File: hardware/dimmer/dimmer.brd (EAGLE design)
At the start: 112.1 x 40.6 mm, 34 parts, among them IC1 MEGA48/88/168-PU, IC2 RFM12, IC3 7812L, IC4 LP2950Z, K1 G5LE, T1 BC547, T2 BC547, X1 AC In, X2 DIM Out, X3 AC Out

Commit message: update labels
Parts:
- D1, D2, D3, D4, D5, D6: value 1N4148DO35-7 -> 1N4148
- JP3: value TX -> PD1/TX
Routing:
- net N$19: track 47.0 -> 48.3 mm
- added copper zone on layer 1, net GND
- added copper zone on layer 16, net GND
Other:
- board text added: "+"
- board text added: "Dimmer 1"
- board text removed: "Dimmer"

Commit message: Use 1k3 instead of 1k2 resistor (0,1%), which is more common. Adopt lookup table accordingly. Change power off timeout to 3s.
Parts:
- C3: value 220n -> 100µ; device rcl:C025-030X050 -> rcl:E1,8-4
- F1: value F50mA -> T50mA; device fuse:GSH15 -> fuse:SH22,5
- IC1: value MEGA48/88/168-PU -> MEGA328PU
- R3: value 1k2 -> 1k3
- moved F1 5.09 mm to (8.57, 15.2)
- moved X3 2.54 mm to (0.00, 25.4)
- moved X1 2.54 mm to (0.00, 15.2)
- moved C2 1.27 mm to (62.2, 12.7), turned to 180 degrees
- turned C3 to 180 degrees
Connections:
- net GND: now also C3.-; no longer C3.2
- net N$9: now also C3.+; no longer C3.1
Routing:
- net N$19: track 48.3 -> 31.4 mm
- net N$22: track 54.6 -> 62.2 mm
- net GND: track 271.6 -> 277.2 mm
- net N$17: track 96.2 -> 91.9 mm
- net N$23: track 18.0 -> 13.9 mm
- net N$9: track 56.8 -> 55.4 mm
- net N$21: track 26.1 -> 25.0 mm
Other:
- board text added: "-"
- board text added: "1"
- board text added: "L"
- board text added: "N"

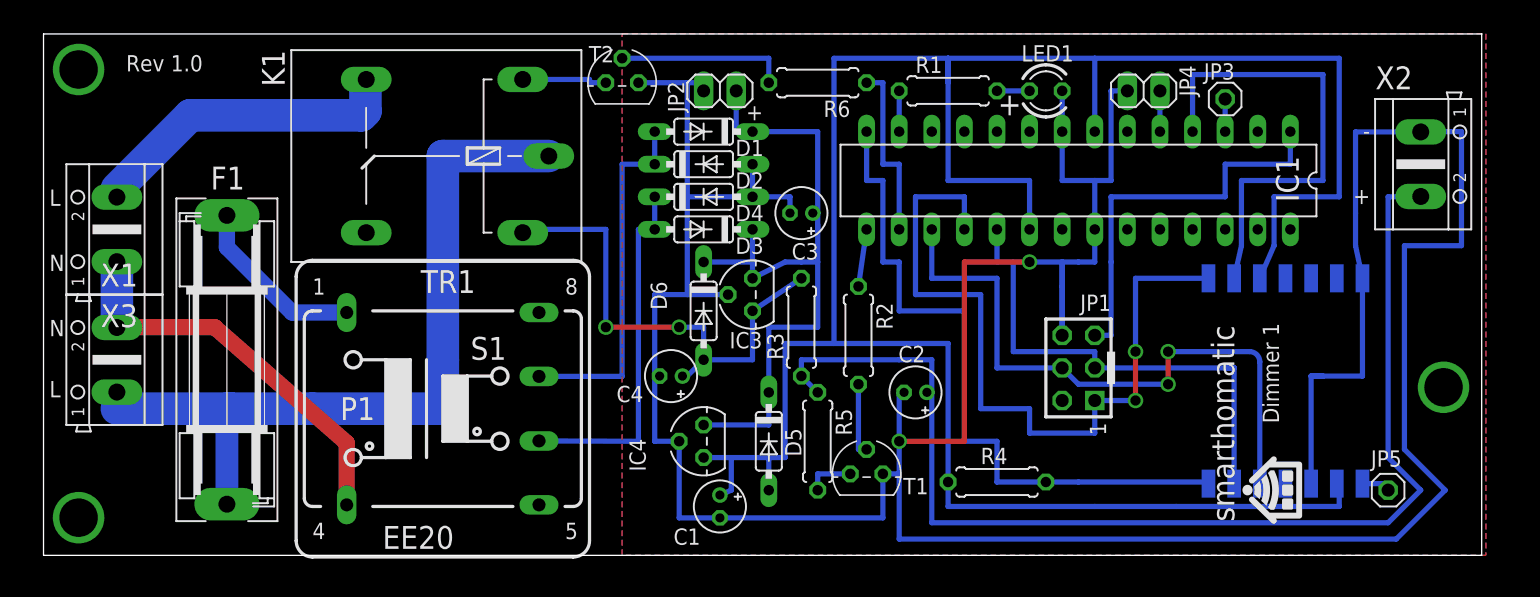
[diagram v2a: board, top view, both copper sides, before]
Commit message: minor movement of labels
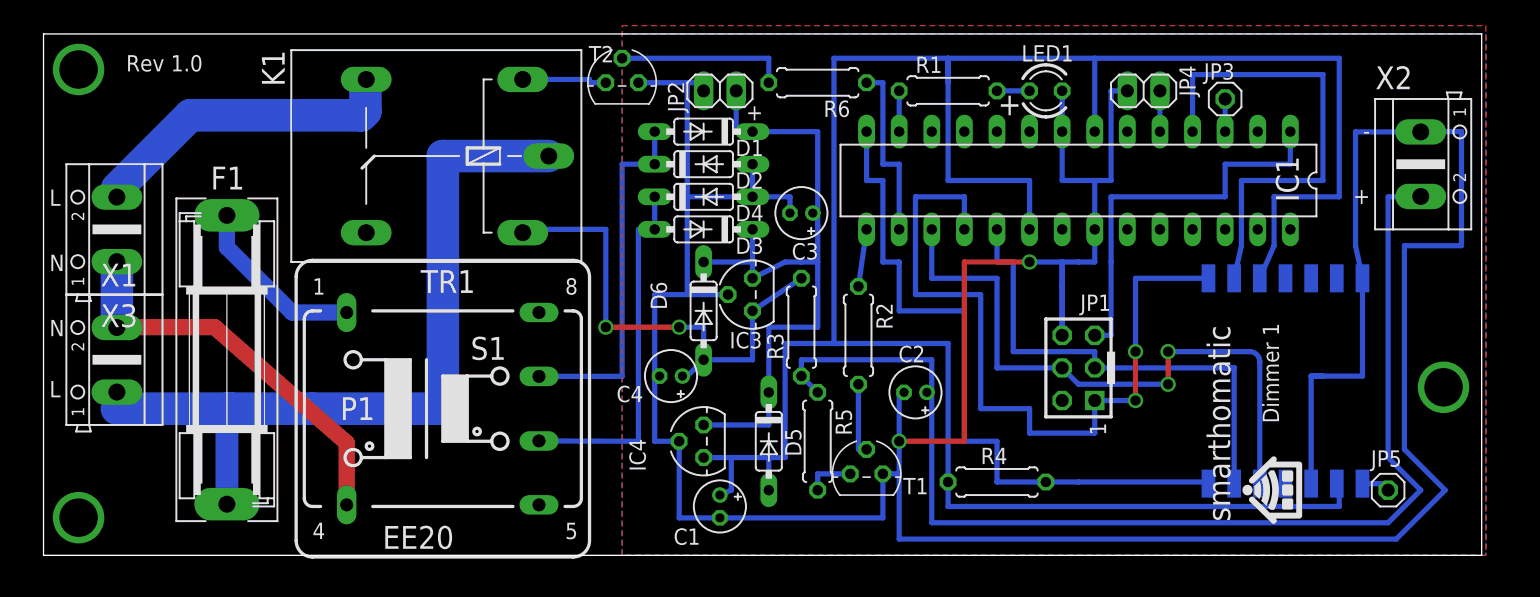
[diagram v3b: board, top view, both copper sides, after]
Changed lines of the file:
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@@
 <wire x1="106.35" y1="40.63" x2="-5.715" y2="40.63" width="0" layer="20"/>
 <wire x1="-5.715" y1="40.63" x2="-5.715" y2="0" width="0" layer="20"/>
-<text x="87.07771875" y="2.628665625" size="1.778" layer="25" font="vector" rot="R90">smarthomatic</text>
+<text x="86.76021875" y="2.628665625" size="1.778" layer="25" font="vector" rot="R90">smarthomatic</text>
 <text x="90.556909375" y="10.297490625" size="1.27" layer="25" font="vector" rot="R90">Dimmer 1</text>
 <text x="0.7179" y="37.7094375" size="1.27" layer="25" font="vector">Rev 1.0</text>
@@
 </class>
 </classes>
-<designrules name="default">
+<designrules name="Fusion_eagle_rule_v1.1">
 <description language="de">&lt;b&gt;EAGLE Design Rules&lt;/b&gt;
 &lt;p&gt;
@@
 necessary adjustments and save your customized
 design rules under a new name.</description>
+<description language="zh">&lt;b&gt;Seeed Studio EAGLE Design Rules&lt;/b&gt;
+</description>
 <param name="layerSetup" value="(1*16)"/>
 <param name="mtCopper" value="0.035mm 0.035mm 0.035mm 0.035mm 0.035mm 0.035mm 0.035mm 0.035mm 0.035mm 0.035mm 0.035mm 0.035mm 0.035mm 0.035mm 0.035mm 0.035mm"/>
 <param name="mtIsolate" value="1.5mm 0.15mm 0.2mm 0.15mm 0.2mm 0.15mm 0.2mm 0.15mm 0.2mm 0.15mm 0.2mm 0.15mm 0.2mm 0.15mm 0.2mm"/>
-<param name="mdWireWire" value="8mil"/>
-<param name="mdWirePad" value="8mil"/>
-<param name="mdWireVia" value="8mil"/>
-<param name="mdPadPad" value="8mil"/>
-<param name="mdPadVia" value="8mil"/>
-<param name="mdViaVia" value="8mil"/>
-<param name="mdSmdPad" value="8mil"/>
-<param name="mdSmdVia" value="8mil"/>
-<param name="mdSmdSmd" value="8mil"/>
+<param name="mdWireWire" value="6mil"/>
+<param name="mdWirePad" value="6mil"/>
+<param name="mdWireVia" value="6mil"/>
+<param name="mdPadPad" value="6mil"/>
+<param name="mdPadVia" value="6mil"/>
+<param name="mdViaVia" value="6mil"/>
+<param name="mdSmdPad" value="0mil"/>
+<param name="mdSmdVia" value="0mil"/>
+<param name="mdSmdSmd" value="0mil"/>
 <param name="mdViaViaSameLayer" value="8mil"/>
 <param name="mnLayersViaInSmd" value="2"/>
-<param name="mdCopperDimension" value="40mil"/>
-<param name="mdDrill" value="8mil"/>
+<param name="mdCopperDimension" value="10mil"/>
+<param name="mdDrill" value="10mil"/>
 <param name="mdSmdStop" value="0mil"/>
-<param name="msWidth" value="10mil"/>
-<param name="msDrill" value="24mil"/>
-<param name="msMicroVia" value="9.99mm"/>
+<param name="msWidth" value="6mil"/>
+<param name="msDrill" value="12mil"/>
+<param name="msMicroVia" value="12mil"/>
 <param name="msBlindViaRatio" value="0.5"/>
 <param name="rvPadTop" value="0.25"/>
@@
 <param name="rlMinPadBottom" value="10mil"/>
 <param name="rlMaxPadBottom" value="20mil"/>
-<param name="rlMinViaOuter" value="8mil"/>
+<param name="rlMinViaOuter" value="6mil"/>
 <param name="rlMaxViaOuter" value="20mil"/>
-<param name="rlMinViaInner" value="8mil"/>
+<param name="rlMinViaInner" value="6mil"/>
 <param name="rlMaxViaInner" value="20mil"/>
 <param name="rlMinMicroViaOuter" value="4mil"/>
@@
 <param name="psTop" value="-1"/>
 <param name="psBottom" value="-1"/>
-<param name="psFirst" value="-1"/>
+<param name="psFirst" value="0"/>
 <param name="psElongationLong" value="100"/>
 <param name="psElongationOffset" value="100"/>
 <param name="mvStopFrame" value="1"/>
 <param name="mvCreamFrame" value="0"/>
-<param name="mlMinStopFrame" value="4mil"/>
-<param name="mlMaxStopFrame" value="4mil"/>
+<param name="mlMinStopFrame" value="2mil"/>
+<param name="mlMaxStopFrame" value="2mil"/>
 <param name="mlMinCreamFrame" value="0mil"/>
 <param name="mlMaxCreamFrame" value="0mil"/>
-<param name="mlViaStopLimit" value="0mil"/>
+<param name="mlViaStopLimit" value="100mil"/>
 <param name="srRoundness" value="0"/>
 <param name="srMinRoundness" value="0mil"/>
@@
 <param name="checkAngle" value="0"/>
 <param name="checkFont" value="1"/>
-<param name="checkRestrict" value="1"/>
+<param name="checkRestrict" value="0"/>
 <param name="useDiameter" value="13"/>
 <param name="maxErrors" value="50"/>
@@
 </polygon>
 <polygon width="0.4064" layer="1" isolate="0.4064">
-<vertex x="39.37" y="40.64"/>
-<vertex x="106.68" y="40.64"/>
+<vertex x="39.37" y="41.275"/>
+<vertex x="106.68" y="41.275"/>
 <vertex x="106.68" y="0"/>
 <vertex x="39.37" y="0"/>

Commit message: label added
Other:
- board text added: ">14.5V="
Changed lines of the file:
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@@
 <text x="86.76021875" y="2.628665625" size="1.778" layer="25" font="vector" rot="R90">smarthomatic</text>
 <text x="90.556909375" y="10.297490625" size="1.27" layer="25" font="vector" rot="R90">Dimmer 1</text>
-<text x="0.7179" y="37.7094375" size="1.27" layer="25" font="vector">Rev 1.0</text>
+<text x="0.7179" y="37.7094375" size="1.27" layer="25">Rev 1.0</text>
 <text x="70.485" y="34.29" size="1.778" layer="25" rot="MR0">+</text>
 <rectangle x1="92.317196875" y1="3.091375" x2="92.398196875" y2="3.09715625" layer="25" rot="R90"/>
@@
 <rectangle x1="87.656653125" y1="5.082971875" x2="87.760853125" y2="5.088759375" layer="25" rot="R90"/>
 <text x="-5.260009375" y="12.313090625" size="1.27" layer="25">L</text>
-<text x="49.032490625" y="33.903090625" size="1.27" layer="25" font="vector">+</text>
+<text x="49.032490625" y="37.078090625" size="1.27" layer="25" font="vector">+</text>
 <text x="75.813090625" y="10.340009375" size="1.27" layer="25" rot="R270">1</text>
 <rectangle x1="77.1525" y1="13.335" x2="77.7875" y2="15.875" layer="21"/>
@@
 <text x="-5.260009375" y="22.155590625" size="1.27" layer="25">N</text>
 <text x="-5.260009375" y="27.235590625" size="1.27" layer="25">L</text>
+<text x="43.317490625" y="38.348090625" size="1.27" layer="25">&gt;14.5V=</text>
 </plain>
 <attributes>
@@
 </element>
 <element name="JP3" library="pinhead" package="1X01" value="PD1/TX" x="86.36" y="35.56" smashed="yes">
-<attribute name="NAME" x="84.6963" y="37.0713" size="1.27" layer="25" ratio="10"/>
-<attribute name="VALUE" x="87.9475" y="34.925" size="1.27" layer="27"/>
+<attribute name="NAME" x="88.1888" y="35.1663" size="1.27" layer="25" ratio="10"/>
+<attribute name="VALUE" x="84.7725" y="37.7825" size="1.27" layer="27"/>
 </element>
 <element name="JP4" library="pinhead" package="1X02" value="On/Off" x="80.01" y="36.195" smashed="yes">
-<attribute name="NAME" x="82.7913" y="38.1762" size="1.27" layer="25" ratio="10" rot="R270"/>
-<attribute name="VALUE" x="82.55" y="39.37" size="1.27" layer="27" rot="R180"/>
+<attribute name="NAME" x="83.1088" y="37.5412" size="1.27" layer="25" ratio="10" rot="R270"/>
+<attribute name="VALUE" x="77.47" y="38.4175" size="1.27" layer="27"/>
 </element>
 <element name="F1" library="fuse" package="SH22,5" value="T50mA" x="8.5725" y="15.24" smashed="yes" rot="R90">
